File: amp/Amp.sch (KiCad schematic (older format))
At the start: 25 parts

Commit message: updated amp schematic with glue
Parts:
- added C?: 1u, symbol Device:C
- added J?: ACV_Jack, symbol Connector:AudioJack2_Ground_Switch
- added J? (x4): AIN4_Jack, symbol Connector:AudioJack2_Ground_Switch
- added J?: BCV_Jack, symbol Connector:AudioJack2_Ground_Switch
- added J?: MAIN_OUT, symbol Connector:AudioJack3
- added J?: HP_OUT, symbol Connector:AudioJack3
- added R? (x4): 10K, symbol Device:R
- added R? (x2): R, symbol Device:R
- added RV? (x4): 47K, symbol Device:R_POT
- added RV?: MASTER_VOL_A, symbol Device:R_POT_Dual_Separate
- added RV?: MASTER_VOL_B, symbol Device:R_POT_Dual_Separate
- added SW? (x2): SW_DPDT_x2, symbol Switch:SW_DPDT_x2
- added U? (x2): TL072, symbol Amplifier_Operational:TL072
- added U?: LM13700, symbol Amplifier_Operational:LM13700
- R?: value 470K -> 100K
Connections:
- net labels added: AIN1, AIN2, AIN3, AIN4, B_CV, B_OUT, CV_DEFALT_TODO_ZERO_OR_10?
- net labels removed: A_IN
- wire segments 78 -> 198
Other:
- note added: "MIXDOWN"
- note added: "TODO remaining opamp could be inverter from CVA to CVB\nparams require design since input is not zero-centered"
- note added: "TODO should there even be a HP out? kinda redundant, might conflict if 2"
- moved on the sheet: C?, R?, U?A, U?B, U?C, U?E

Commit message: updated VCA based on new calculations
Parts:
- removed C?: 1u, symbol Device:C
- removed R? (x3): R, symbol Device:R
- removed R?: 150K, symbol Device:R
- removed R?: 100K, symbol Device:R
- removed R?: 220K, symbol Device:R
- removed RV?: 10K, symbol Amp-rescue:POT
- removed U?: TL072, symbol Amplifier_Operational:TL072
- removed U?: LM13700, symbol Amplifier_Operational:LM13700
- added R?: 150K, symbol Device:R
- added U?: LM13700, symbol Amplifier_Operational:LM13700
- R?: value 5K6 -> 7K5
- R?: value 1K -> 3K3
- R?: value 100K -> 820K
- R?: value 5K6 -> 1K8
- RV? (x4): value 47K -> 100K
- RV?: value MASTER_VOL_A -> MASTER_VOL_A_10K
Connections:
- net labels added: AIN_MIX, AIN_SUM, BIN_MIX, BIN_SUM
- net labels removed: B_OUT, CV_DEFALT_TODO_ZERO_OR_10?
- wire segments 198 -> 177
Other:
- note added: "+- 5V Signal"
- note added: "-18mV/V"
- note added: "100mV/V * 40mV/V = 4mV/V\n5V -> 20mV"
- note added: "Default CV = 4.8V"
- note added: "IREF=1mA"
- note added: "Limit IABC to 1.52mA"
- note added: "Subtract 5V from CV"
- moved on the sheet: C?, R?, RV?A, RV?B, U?B

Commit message: added notes
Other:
- note added: "TODO: this might be a backwards mirror, that starts at IREF\nand adds exponentially. If that’s the case, instead we should\nswitch to a NPN design, and then use a PNP current mirror to\nmirror the current to positive. That might simplify the CV\nscale stage, which I suspect is also backwards."
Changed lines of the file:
@@
 Wire Wire Line
 	3450 4500 5050 4500
+Text Notes 7900 2700 0    50   ~ 0
+TODO: this might be a backwards mirror, that starts at IREF\nand adds exponentially. If that’s the case, instead we should\nswitch to a NPN design, and then use a PNP current mirror to\nmirror the current to positive. That might simplify the CV\nscale stage, which I suspect is also backwards.
 $EndSCHEMATC

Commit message: got working amplifier
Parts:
- removed Q? (x2): 2N3906, Package_TO_SOT_THT:TO-92_Inline, symbol Transistor_BJT:2N3906
- added Q? (x2): DMMT5401, KiCad/kicad-footprints/Package_TO_SOT_SMD.pretty:SOT-23-6, symbol synth:DMMT5401
- R?: value 7K5 -> 5K
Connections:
- wire segments 177 -> 181
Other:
- note added: "5V (G=1) to 0V (G=0)\nCan be overdriven slightly to G=1.2"
- note added: "Limit IABC\nIABC max for LM13700 is 2mA.\nThis set’s IABC max above that,\nbut if we use a higher resistance\nthe exponmential shape falls off\nbefore 1mA"
- note added: "Linear control here if needed"
- note removed: "Limit IABC to 1.52mA"
- note removed: "TODO: this might be a backwards mirror, that starts at IREF\nand adds exponentially. If that’s the case, instead we should\nswitch to a NPN design, and then use a PNP current mirror to\nmirror the current to positive. That might simplify the CV\nscale stage, which I suspect is also backwards."
- moved on the sheet: C?, J?, R?, RV?, RV?B, SW?A, SW?B, U?A, U?B, U?C, U?D, U?E

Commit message: separated amp into sheets
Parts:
- removed C?: 30p, symbol Device:C
- removed C?: 1u, symbol Device:C
- removed J?: ACV_Jack, symbol Connector:AudioJack2_Ground_Switch
- removed J? (x4): AIN4_Jack, symbol Connector:AudioJack2_Ground_Switch
- removed J?: BCV_Jack, symbol Connector:AudioJack2_Ground_Switch
- removed J?: MAIN_OUT, symbol Connector:AudioJack3
- removed J?: HP_OUT, symbol Connector:AudioJack3
- removed Q? (x2): DMMT5401, KiCad/kicad-footprints/Package_TO_SOT_SMD.pretty:SOT-23-6, symbol synth:DMMT5401
- removed R?: 5K, symbol Device:R
- removed R?: 12K, symbol Device:R
- removed R?: R, symbol Device:R
- removed R?: 3K3, symbol Device:R
- removed R?: 820K, symbol Device:R
- removed R?: 1K8, symbol Device:R
- removed R?: 100K, symbol Device:R
- removed R?: 220K, symbol Device:R
- removed R? (x4): 10K, symbol Device:R
- removed R?: 150K, symbol Device:R
- removed RV? (x4): 100K, symbol Device:R_POT
- removed RV?: MASTER_VOL_A_10K, symbol Device:R_POT_Dual_Separate
- removed RV?: MASTER_VOL_B, symbol Device:R_POT_Dual_Separate
- removed SW? (x2): SW_DPDT_x2, symbol Switch:SW_DPDT_x2
- removed U? (x4): LM13700, symbol Amplifier_Operational:LM13700
- removed U? (x6): TL072, symbol Amplifier_Operational:TL072
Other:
- note removed: "+- 5V Signal"
- note removed: "-18mV/V"
- note removed: "100mV/V * 40mV/V = 4mV/V\n5V -> 20mV"
- note removed: "5V (G=1) to 0V (G=0)\nCan be overdriven slightly to G=1.2"
- note removed: "A-VCA"
- note removed: "Default CV = 4.8V"
- note removed: "IREF=1mA"
- note removed: "Limit IABC\nIABC max for LM13700 is 2mA.\nThis set’s IABC max above that,\nbut if we use a higher resistance\nthe exponmential shape falls off\nbefore 1mA"
- note removed: "Linear control here if needed"
- note removed: "MIXDOWN"
- note removed: "Subtract 5V from CV"
- note removed: "TODO remaining opamp could be inverter from CVA to CVB\nparams require design since input is not zero-centered"
- note removed: "TODO should there even be a HP out? kinda redundant, might conflict if 2"

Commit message: reworked amp sheets and notes
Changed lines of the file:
@@
 $Descr A4 11693 8268
 encoding utf-8
-Sheet 1 5
+Sheet 1 3
 Title "VCA Module"
 Date "2020-04-04"
@@
 F1 "AVCA.sch" 50
 $EndSheet
-$Sheet
-S 700  3000 1150 750
-U 5EBC1861
-F0 "BVCA" 50
-F1 "BVCA.sch" 50
-$EndSheet
-$Sheet
-S 700  4000 1150 750
-U 5EC009ED
-F0 "OutputStage" 50
-F1 "OutputStage.sch" 50
-$EndSheet
 $EndSCHEMATC

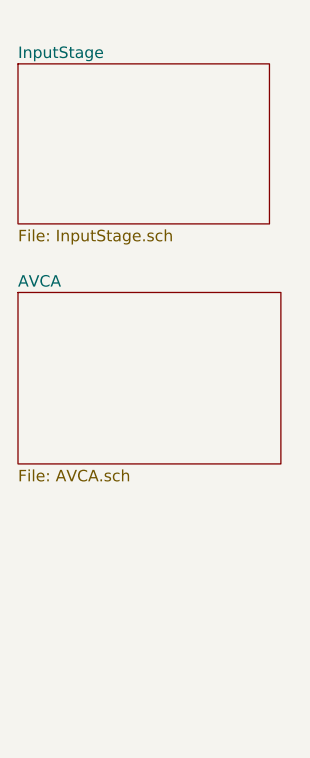
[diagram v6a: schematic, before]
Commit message: update amp config for quad-cascade design
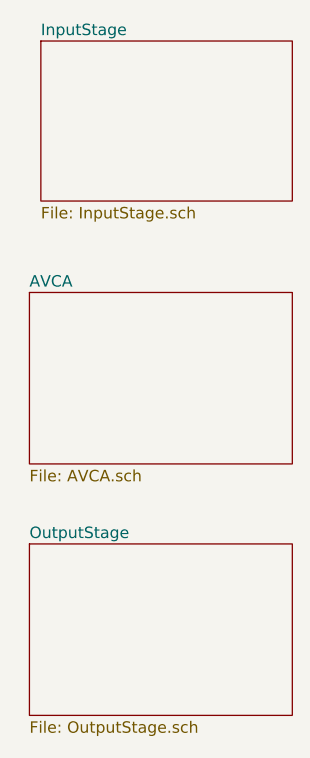
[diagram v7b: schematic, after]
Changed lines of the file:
@@
 $Descr A4 11693 8268
 encoding utf-8
-Sheet 1 3
+Sheet 1 4
 Title "VCA Module"
 Date "2020-04-04"
@@
 $EndDescr
 $Sheet
-S 700  1000 1100 700
+S 800  900  1100 700
 U 5EB23D44
 F0 "InputStage" 50
@@
 $EndSheet
 $Sheet
-S 700  2000 1150 750
+S 750  2000 1150 750
 U 5EBA9693
 F0 "AVCA" 50
 F1 "AVCA.sch" 50
 $EndSheet
+$Sheet
+S 750  3100 1150 750
+U 5EC4DE09
+F0 "OutputStage" 50
+F1 "OutputStage.sch" 50
+$EndSheet
 $EndSCHEMATC

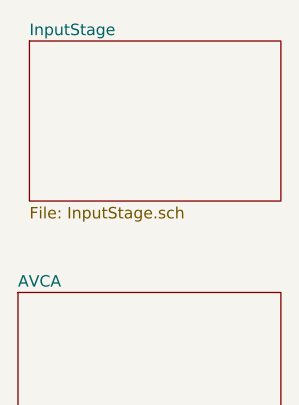
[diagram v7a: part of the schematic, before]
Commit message: add eurorack connector, fix some issues
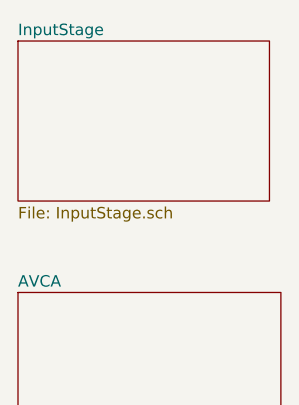
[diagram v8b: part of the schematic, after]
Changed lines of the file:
@@
 $EndDescr
 $Sheet
-S 800  900  1100 700
+S 750  900  1100 700
 U 5EB23D44
 F0 "InputStage" 50
